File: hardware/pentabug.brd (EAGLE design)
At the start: 160 x 100 mm, 13 parts, among them IC1 ATMEGA88

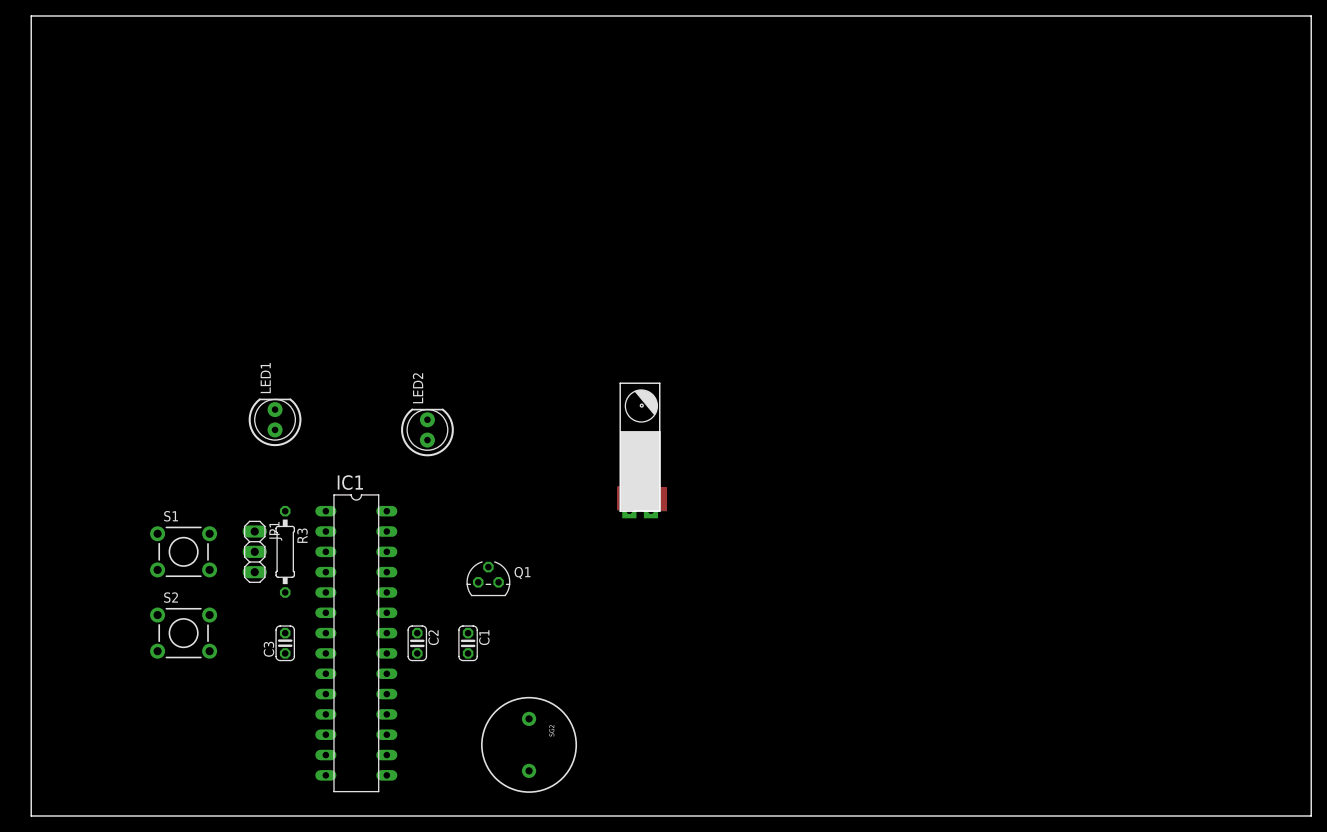
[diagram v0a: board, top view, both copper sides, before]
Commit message: added battery holder, bord layout changed to reflect later constellation of components
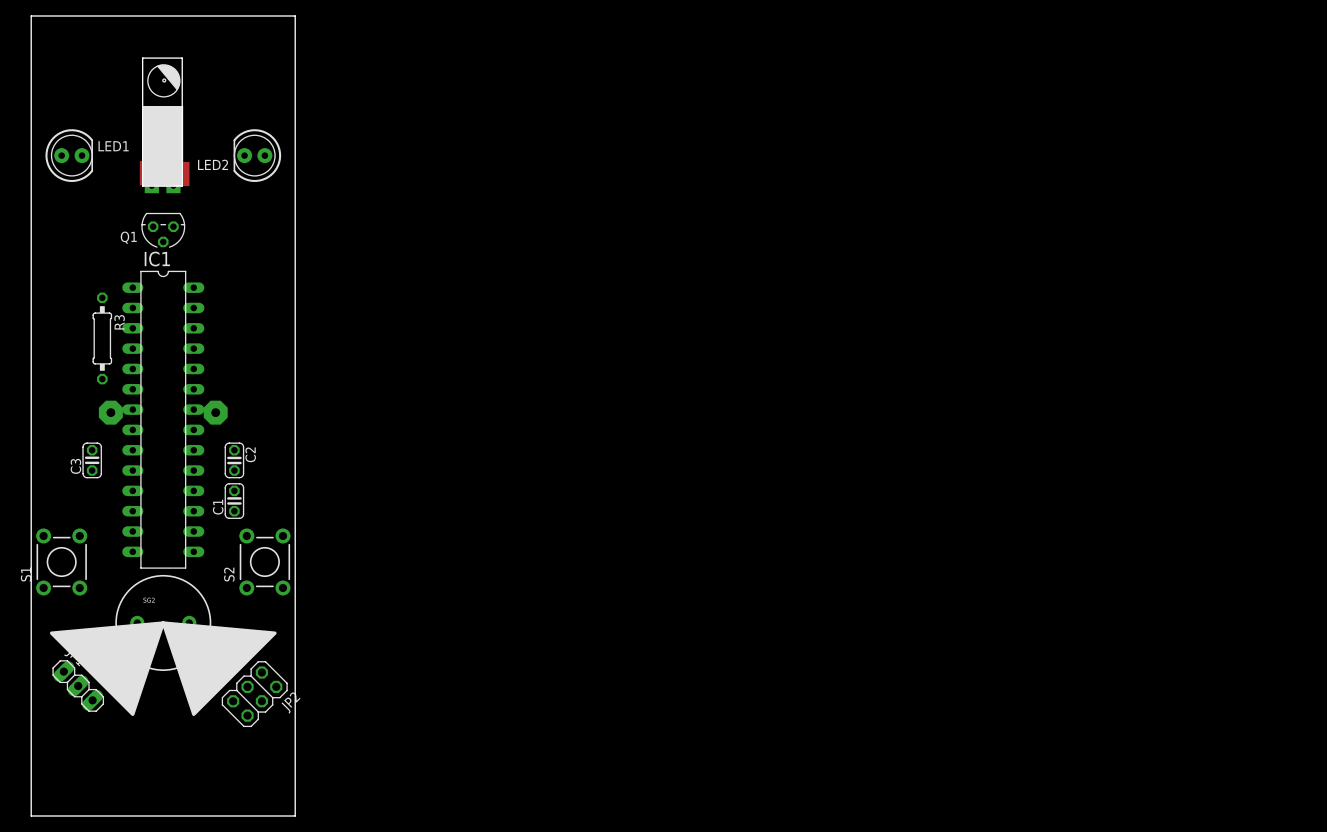
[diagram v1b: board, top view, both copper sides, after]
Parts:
- added BAT1: BATTERY_2XAAA, seb:BATTERY_2XAAA
- added JP2: (no value), pinhead:2X03
- moved U$1 72.2 mm to (17.8, 78.7)
- moved Q1 60.2 mm to (16.5, 73.7), turned to 180 degrees
- moved SG2 48.2 mm to (16.5, 24.1), turned to 0 degrees
- moved LED1 41.7 mm to (5.08, 82.5), turned to 0 degrees
- moved LED2 40.5 mm to (27.9, 82.5), turned to 180 degrees
- moved IC1 36.9 mm to (16.5, 49.5)
- moved R3 35.1 mm to (8.89, 59.7)
- moved C1 34.2 mm to (25.4, 39.4), turned to 90 degrees
- moved C3 33.2 mm to (7.62, 44.5)
- moved C2 32.3 mm to (25.4, 44.5)
- moved JP1 27.7 mm to (5.88, 16.2), turned to 315 degrees
- moved S1 15.3 mm to (3.81, 31.8), turned to 90 degrees
- moved S2 13.5 mm to (29.2, 31.8), turned to 90 degrees
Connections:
- removed net N$2: IC1.1, R3.1
- new net MISO: IC1.18, JP2.1
- new net MOSI: IC1.17, JP2.4
- new net RST: IC1.1, JP2.5, R3.1
- new net SCK: IC1.19, JP2.3
- net GND: now also BAT1.-, JP2.6
- net VCC: now also BAT1.+
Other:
- board size 160 x 100 mm -> 33 x 100 mm

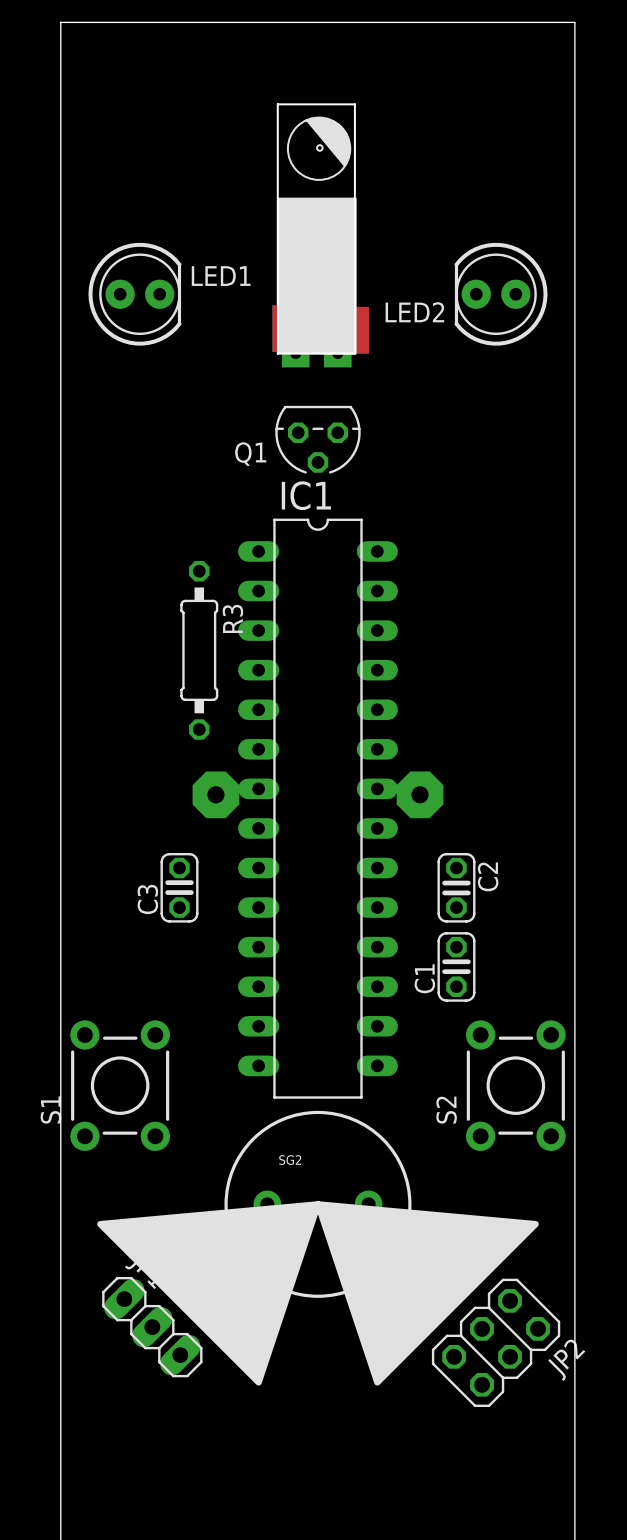
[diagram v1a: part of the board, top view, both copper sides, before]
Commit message: some routing, buzzer footprint still wrong
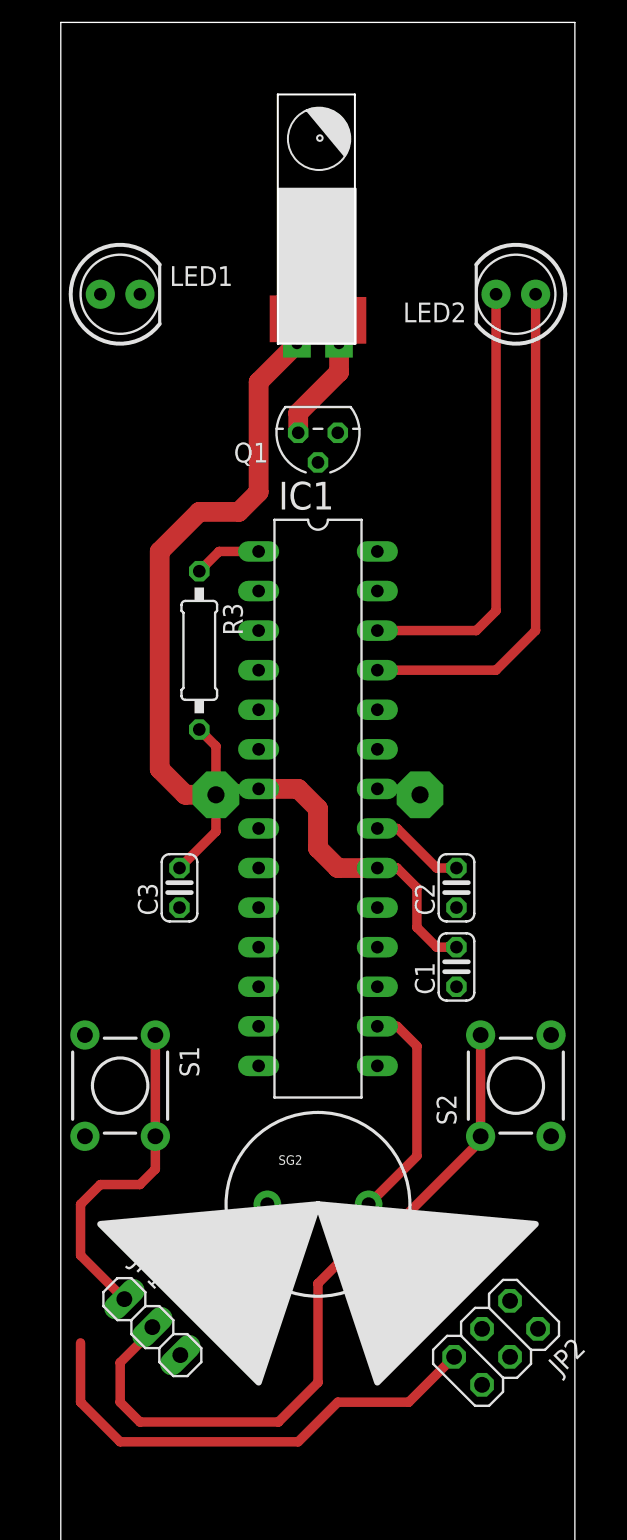
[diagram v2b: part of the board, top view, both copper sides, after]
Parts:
- moved U$1 7.73 mm to (16.5, 86.4)
- moved LED1 1.27 mm to (3.81, 82.5)
- moved LED2 1.27 mm to (29.2, 82.5)
- turned C2 to 90 degrees
- turned S1 to 270 degrees
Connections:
- net N$8: now also U$1.P$2; no longer U$1.P$1
- net VCC: now also U$1.P$1; no longer U$1.P$2
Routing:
- net VCC: track 0.00 -> 69.8 mm
- net TX: track 0.00 -> 47.3 mm
- net RST: track 0.00 -> 35.4 mm
- net N$5: track 0.00 -> 32.8 mm
- net N$11: track 0.00 -> 28.5 mm
- net RX: track 0.00 -> 21.6 mm
- net BUZZR: track 0.00 -> 14.5 mm
- net N$8: track 0.00 -> 6.80 mm
- net N$17: track 0.00 -> 6.13 mm
